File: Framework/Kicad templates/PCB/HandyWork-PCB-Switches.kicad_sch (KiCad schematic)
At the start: 0 parts

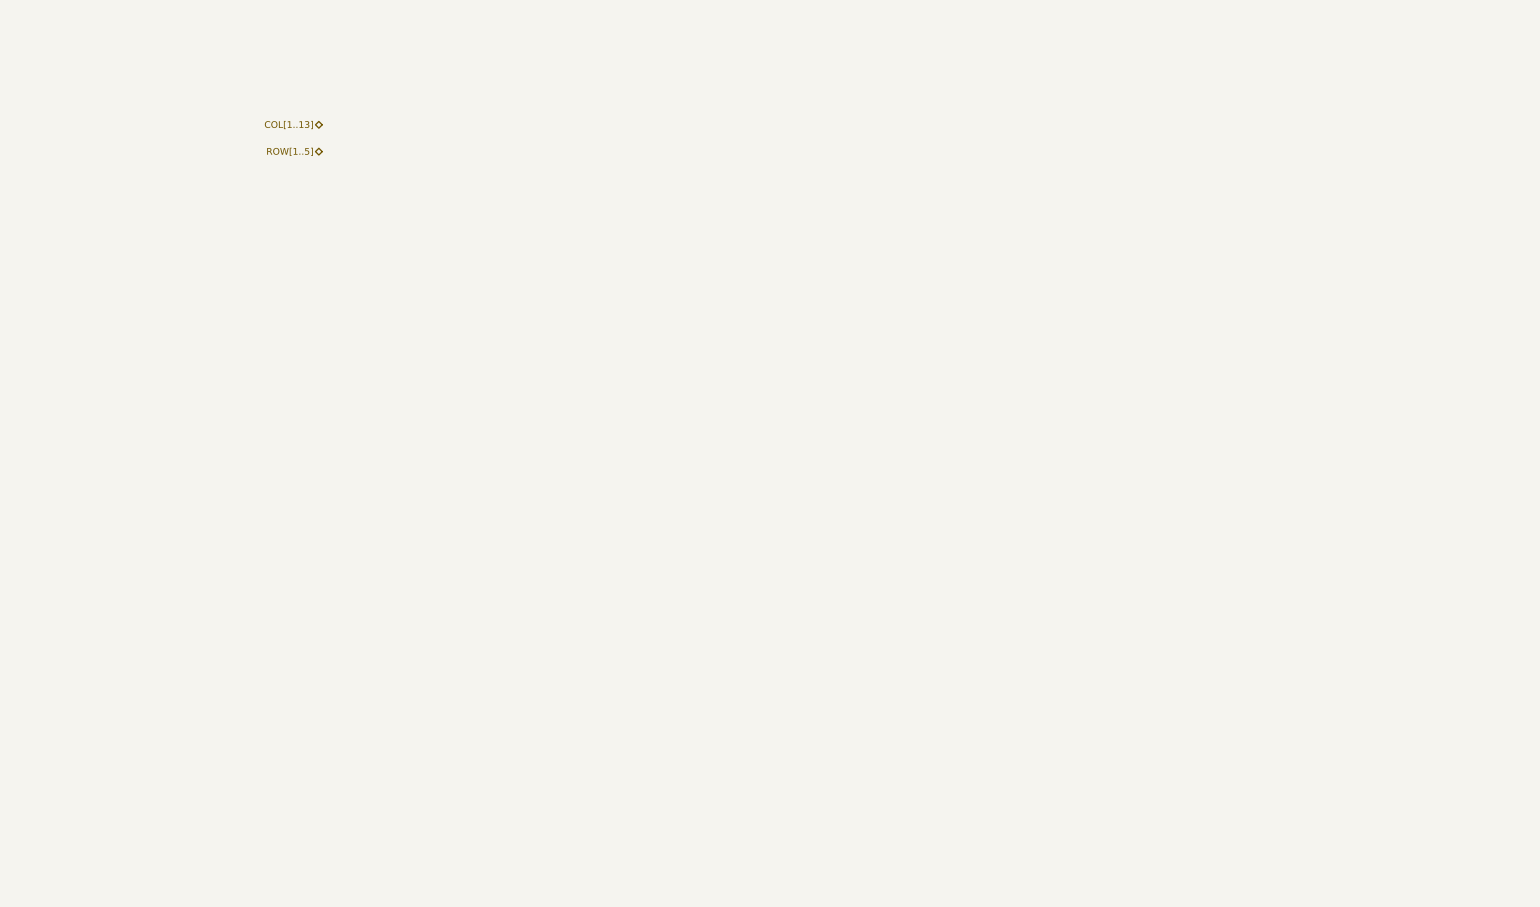
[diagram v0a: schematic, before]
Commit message: HandyWork: Updating KiCad PCB template. Now complete.
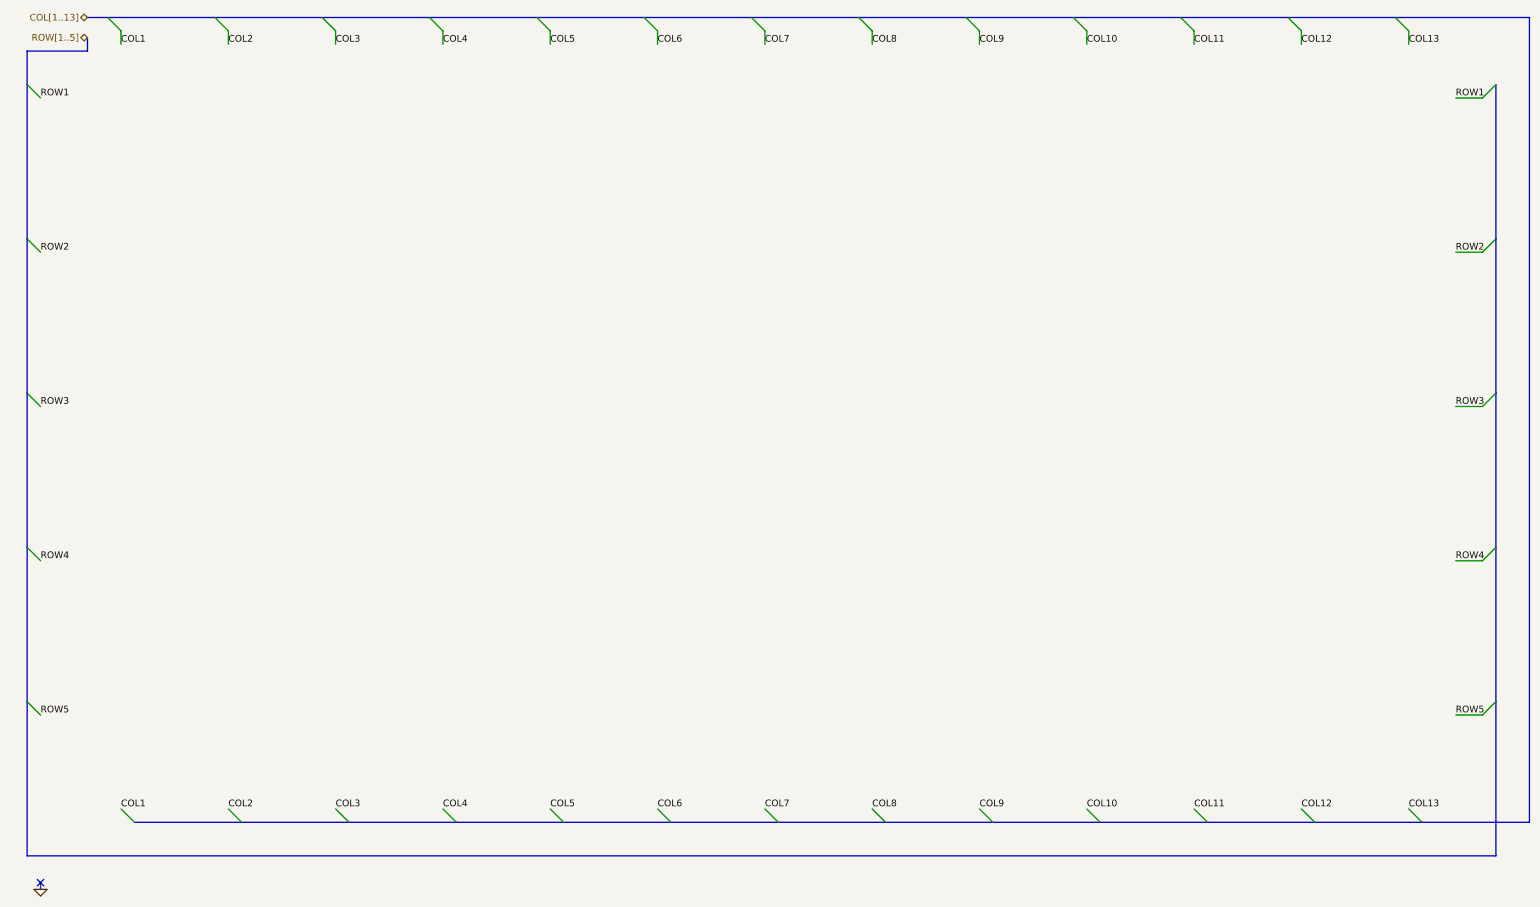
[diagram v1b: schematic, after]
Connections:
- no-connect marks 0 -> 1
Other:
- company: (none) -> Axel Voitier
- title: (none) -> HandyWork - PCB Template
